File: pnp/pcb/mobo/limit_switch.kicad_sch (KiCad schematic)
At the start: 6 parts, among them J2 X_LIMIT

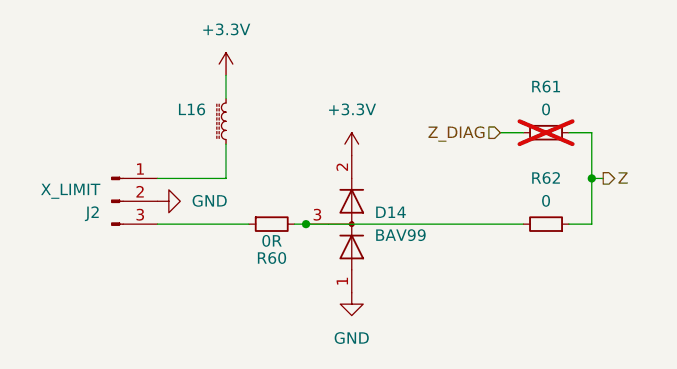
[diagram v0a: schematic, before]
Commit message: Replaced solder jumpers with 0ohm
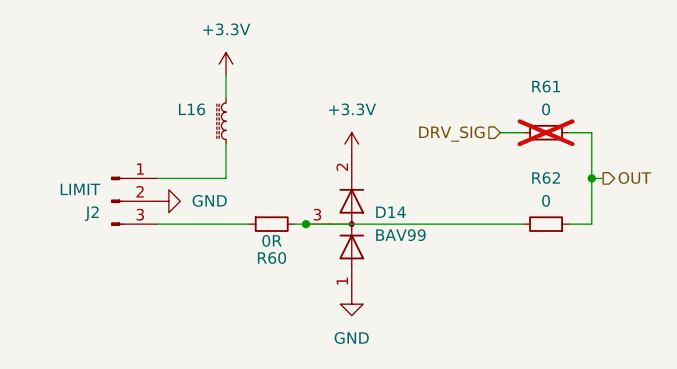
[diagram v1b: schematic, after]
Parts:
- J2: value X_LIMIT -> LIMIT
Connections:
- net Z renamed OUT
- net Z_DIAG renamed DRV_SIG
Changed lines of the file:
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@@
     (stroke (width 0) (type default))
   )
-  (hierarchical_label "Z_DIAG" (shape input) (at 123.19 63.5 180) (fields_autoplaced)
+  (hierarchical_label "DRV_SIG" (shape input) (at 123.19 63.5 180) (fields_autoplaced)
     (effects (font (size 1.27 1.27)) (justify right))
   )
-  (hierarchical_label "Z" (shape output) (at 134.62 68.58 0) (fields_autoplaced)
+  (hierarchical_label "OUT" (shape output) (at 134.62 68.58 0) (fields_autoplaced)
     (effects (font (size 1.27 1.27)) (justify left))
   )
@@
           (reference "R61") (unit 1)
         )
+        (path "/7255cbd1-8d38-4545-be9a-7fc5488ef942/0fa977f6-f205-45fb-8cef-faba0ab4196d"
+          (reference "R73") (unit 1)
+        )
+        (path "/7255cbd1-8d38-4545-be9a-7fc5488ef942/b4f37e88-b6f1-47ba-be3f-95aa26d781b3"
+          (reference "R76") (unit 1)
+        )
       )
     )
@@
           (reference "#PWR083") (unit 1)
         )
+        (path "/7255cbd1-8d38-4545-be9a-7fc5488ef942/0fa977f6-f205-45fb-8cef-faba0ab4196d"
+          (reference "#PWR085") (unit 1)
+        )
+        (path "/7255cbd1-8d38-4545-be9a-7fc5488ef942/b4f37e88-b6f1-47ba-be3f-95aa26d781b3"
+          (reference "#PWR0123") (unit 1)
+        )
       )
     )
@@
           (reference "R62") (unit 1)
         )
+        (path "/7255cbd1-8d38-4545-be9a-7fc5488ef942/0fa977f6-f205-45fb-8cef-faba0ab4196d"
+          (reference "R74") (unit 1)
+        )
+        (path "/7255cbd1-8d38-4545-be9a-7fc5488ef942/b4f37e88-b6f1-47ba-be3f-95aa26d781b3"
+          (reference "R77") (unit 1)
+        )
       )
     )
@@
           (reference "#PWR0117") (unit 1)
         )
+        (path "/7255cbd1-8d38-4545-be9a-7fc5488ef942/0fa977f6-f205-45fb-8cef-faba0ab4196d"
+          (reference "#PWR0122") (unit 1)
+        )
+        (path "/7255cbd1-8d38-4545-be9a-7fc5488ef942/b4f37e88-b6f1-47ba-be3f-95aa26d781b3"
+          (reference "#PWR0126") (unit 1)
+        )
       )
     )
@@
         (path "/7255cbd1-8d38-4545-be9a-7fc5488ef942/02705e7d-b250-4955-94ce-1e1db6770300"
           (reference "#PWR0176") (unit 1)
+        )
+        (path "/7255cbd1-8d38-4545-be9a-7fc5488ef942/0fa977f6-f205-45fb-8cef-faba0ab4196d"
+          (reference "#PWR086") (unit 1)
+        )
+        (path "/7255cbd1-8d38-4545-be9a-7fc5488ef942/b4f37e88-b6f1-47ba-be3f-95aa26d781b3"
+          (reference "#PWR0124") (unit 1)
         )
       )
@@
         (path "/7255cbd1-8d38-4545-be9a-7fc5488ef942/02705e7d-b250-4955-94ce-1e1db6770300"
           (reference "D14") (unit 1)
+        )
+        (path "/7255cbd1-8d38-4545-be9a-7fc5488ef942/0fa977f6-f205-45fb-8cef-faba0ab4196d"
+          (reference "D15") (unit 1)
+        )
+        (path "/7255cbd1-8d38-4545-be9a-7fc5488ef942/b4f37e88-b6f1-47ba-be3f-95aa26d781b3"
+          (reference "D16") (unit 1)
         )
       )
@@
           (reference "R60") (unit 1)
         )
+        (path "/7255cbd1-8d38-4545-be9a-7fc5488ef942/0fa977f6-f205-45fb-8cef-faba0ab4196d"
+          (reference "R72") (unit 1)
+        )
+        (path "/7255cbd1-8d38-4545-be9a-7fc5488ef942/b4f37e88-b6f1-47ba-be3f-95aa26d781b3"
+          (reference "R75") (unit 1)
+        )
       )
     )
@@
         (path "/7255cbd1-8d38-4545-be9a-7fc5488ef942/02705e7d-b250-4955-94ce-1e1db6770300"
           (reference "L16") (unit 1)
+        )
+        (path "/7255cbd1-8d38-4545-be9a-7fc5488ef942/0fa977f6-f205-45fb-8cef-faba0ab4196d"
+          (reference "L14") (unit 1)
+        )
+        (path "/7255cbd1-8d38-4545-be9a-7fc5488ef942/b4f37e88-b6f1-47ba-be3f-95aa26d781b3"
+          (reference "L17") (unit 1)
         )
       )
@@
       (effects (font (size 1.27 1.27)) (justify right))
     )
-    (property "Value" "X_LIMIT" (at 78.74 69.85 0)
+    (property "Value" "LIMIT" (at 78.74 69.85 0)
       (effects (font (size 1.27 1.27)) (justify right))
     )
@@
           (reference "J2") (unit 1)
         )
+        (path "/7255cbd1-8d38-4545-be9a-7fc5488ef942/0fa977f6-f205-45fb-8cef-faba0ab4196d"
+          (reference "J3") (unit 1)
+        )
+        (path "/7255cbd1-8d38-4545-be9a-7fc5488ef942/b4f37e88-b6f1-47ba-be3f-95aa26d781b3"
+          (reference "J4") (unit 1)
+        )
       )
     )
@@
           (reference "#PWR084") (unit 1)
         )
-      )
+        (path "/7255cbd1-8d38-4545-be9a-7fc5488ef942/0fa977f6-f205-45fb-8cef-faba0ab4196d"
+          (reference "#PWR0121") (unit 1)
+        )
+        (path "/7255cbd1-8d38-4545-be9a-7fc5488ef942/b4f37e88-b6f1-47ba-be3f-95aa26d781b3"
+          (reference "#PWR0125") (unit 1)
+        )
+      )

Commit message: Motor driver new Symbol and fix TVS placement
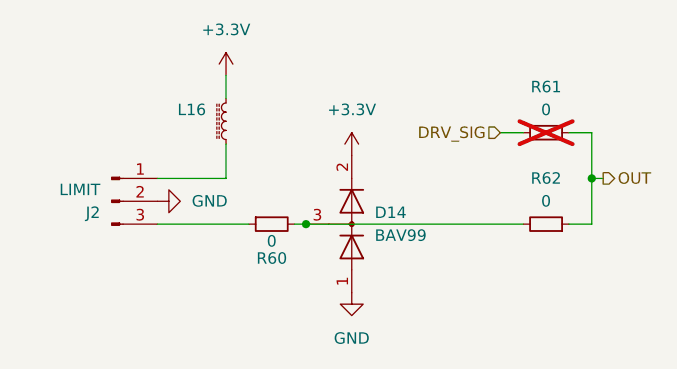
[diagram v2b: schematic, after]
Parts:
- L16: footprint index:L_0805_2012Metric -> Inductor_SMD:L_0805_2012Metric
- R60: value 0R -> 0
- R61, R62: footprint (none) -> Resistor_SMD:R_0805_2012Metric

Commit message: Increased motor driver sense resistor package size
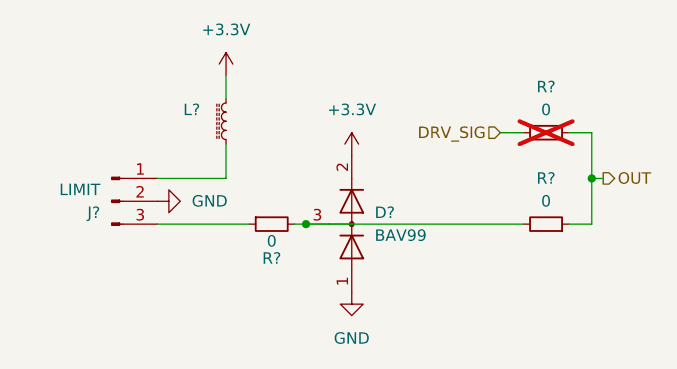
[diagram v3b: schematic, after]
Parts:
- renumbered D14 to D?, J2 to J?, L16 to L?, R61 to R?, R62 to R?, R60 to R?
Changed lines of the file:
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@@
   (symbol (lib_id "Device:R_Small") (at 128.27 63.5 270) (mirror x) (unit 1)
     (in_bom yes) (on_board yes) (dnp yes) (fields_autoplaced)
-    (property "Reference" "R61" (at 128.27 58.42 90)
+    (property "Reference" "R?" (at 128.27 58.42 90)
       (effects (font (size 1.27 1.27)))
     )
@@
   (symbol (lib_name "GND_2") (lib_id "power:GND") (at 85.09 71.12 90) (mirror x) (unit 1)
     (in_bom yes) (on_board yes) (dnp no) (fields_autoplaced)
-    (property "Reference" "#PWR083" (at 91.44 71.12 0)
+    (property "Reference" "#PWR?" (at 91.44 71.12 0)
       (effects (font (size 1.27 1.27)) hide)
     )
@@
   (symbol (lib_id "Device:R_Small") (at 128.27 73.66 270) (mirror x) (unit 1)
     (in_bom yes) (on_board yes) (dnp no) (fields_autoplaced)
-    (property "Reference" "R62" (at 128.27 68.58 90)
+    (property "Reference" "R?" (at 128.27 68.58 90)
       (effects (font (size 1.27 1.27)))
     )
@@
   (symbol (lib_name "GND_1") (lib_id "power:GND") (at 106.68 81.28 0) (mirror y) (unit 1)
     (in_bom yes) (on_board yes) (dnp no) (fields_autoplaced)
-    (property "Reference" "#PWR0117" (at 106.68 87.63 0)
+    (property "Reference" "#PWR?" (at 106.68 87.63 0)
       (effects (font (size 1.27 1.27)) hide)
     )
@@
   (symbol (lib_name "+3.3V_1") (lib_id "power:+3.3V") (at 92.71 57.15 0) (mirror y) (unit 1)
     (in_bom yes) (on_board yes) (dnp no) (fields_autoplaced)
-    (property "Reference" "#PWR0176" (at 92.71 60.96 0)
+    (property "Reference" "#PWR?" (at 92.71 60.96 0)
       (effects (font (size 1.27 1.27)) hide)
     )
@@
   (symbol (lib_id "Diode:BAV99") (at 106.68 73.66 270) (mirror x) (unit 1)
     (in_bom yes) (on_board yes) (dnp no) (fields_autoplaced)
-    (property "Reference" "D14" (at 109.22 72.39 90)
+    (property "Reference" "D?" (at 109.22 72.39 90)
       (effects (font (size 1.27 1.27)) (justify left))
     )
@@
   (symbol (lib_id "Device:R_Small") (at 97.79 73.66 90) (mirror x) (unit 1)
     (in_bom yes) (on_board yes) (dnp no)
-    (property "Reference" "R60" (at 97.79 77.47 90)
+    (property "Reference" "R?" (at 97.79 77.47 90)
       (effects (font (size 1.27 1.27)))
     )
@@
   (symbol (lib_id "Device:L_Ferrite_Small") (at 92.71 62.23 0) (mirror y) (unit 1)
     (in_bom yes) (on_board yes) (dnp no)
-    (property "Reference" "L16" (at 88.9 60.96 0)
+    (property "Reference" "L?" (at 88.9 60.96 0)
       (effects (font (size 1.27 1.27)))
     )
@@
   (symbol (lib_id "Connector:Conn_01x03_Male") (at 80.01 71.12 0) (unit 1)
     (in_bom yes) (on_board yes) (dnp no)
-    (property "Reference" "J2" (at 78.74 72.39 0)
+    (property "Reference" "J?" (at 78.74 72.39 0)
       (effects (font (size 1.27 1.27)) (justify right))
     )
@@
   (symbol (lib_name "+3.3V_1") (lib_id "power:+3.3V") (at 106.68 66.04 0) (mirror y) (unit 1)
     (in_bom yes) (on_board yes) (dnp no) (fields_autoplaced)
-    (property "Reference" "#PWR084" (at 106.68 69.85 0)
-      (effects (font (size 1.27 1.27)) hide)
-    )
+    (property "Reference" "#PWR?" (at 106.68 69.85 0)
+      (effects (font (size 1.27 1.27)) hide)
+    )

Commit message: Mobo parts sourced
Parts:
- removed R?: 0, Resistor_SMD:R_0805_2012Metric, symbol Device:R_Small
- D?: JLCPCB (none) -> C2500; LCSC (none) -> C916421
- J?: JLCPCB C2316 -> C2845452; LCSC C2316 -> C2845452
- L?: JLCPCB (none) -> C1015; LCSC (none) -> C1015; Notes 50Ohm@100Mhz -> (none)
- R? (x2): JLCPCB (none) -> C17477; LCSC (none) -> C17477
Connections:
- net at D?.3 (K), R?.2: now also J?.3 (Pin_3)
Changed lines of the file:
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@@
-    (stroke (width 0) (type default))
-  )
-  (wire (pts (xy 95.25 73.66) (xy 85.09 73.66))
     (stroke (width 0) (type default))
   )
@@
     (stroke (width 0) (type default))
   )
-  (wire (pts (xy 101.6 73.66) (xy 100.33 73.66))
+  (wire (pts (xy 85.09 73.66) (xy 101.6 73.66))
     (stroke (width 0) (type default))
   )
@@
       (effects (font (size 1.27 1.27)) hide)
     )
+    (property "JLCPCB" "C17477" (at 128.27 63.5 0)
+      (effects (font (size 1.27 1.27)) hide)
+    )
+    (property "LCSC" "C17477" (at 128.27 63.5 0)
+      (effects (font (size 1.27 1.27)) hide)
+    )
     (pin "1")
     (pin "2")
@@
       (effects (font (size 1.27 1.27)) hide)
     )
+    (property "JLCPCB" "C17477" (at 128.27 73.66 0)
+      (effects (font (size 1.27 1.27)) hide)
+    )
+    (property "LCSC" "C17477" (at 128.27 73.66 0)
+      (effects (font (size 1.27 1.27)) hide)
+    )
     (pin "1")
     (pin "2")
@@
       (effects (font (size 1.27 1.27)) hide)
     )
+    (property "JLCPCB" "C2500" (at 106.68 73.66 0)
+      (effects (font (size 1.27 1.27)) hide)
+    )
+    (property "LCSC" "C916421" (at 106.68 73.66 0)
+      (effects (font (size 1.27 1.27)) hide)
+    )
     (pin "1")
     (pin "2")
@@
         (path "/7255cbd1-8d38-4545-be9a-7fc5488ef942/b4f37e88-b6f1-47ba-be3f-95aa26d781b3/93becd31-da9a-45fa-a9c6-780d3515a9a1"
           (reference "D16") (unit 1)
-        )
-      )
-    )
-  )
-  (symbol (lib_id "Device:R_Small") (at 97.79 73.66 90) (mirror x) (unit 1)
-    (in_bom yes) (on_board yes) (dnp no)
-    (property "Reference" "R?" (at 97.79 77.47 90)
-      (effects (font (size 1.27 1.27)))
-    )
-    (property "Value" "0" (at 97.79 75.565 90)
-      (effects (font (size 1.27 1.27)))
-    )
-    (property "Footprint" "Resistor_SMD:R_0805_2012Metric" (at 97.79 73.66 0)
-      (effects (font (size 1.27 1.27)) hide)
-    )
-    (property "Datasheet" "~" (at 97.79 73.66 0)
-      (effects (font (size 1.27 1.27)) hide)
-    )
-    (pin "1")
-    (pin "2")
-    (instances
-      (project "mobo"
-        (path "/7255cbd1-8d38-4545-be9a-7fc5488ef942/b4f37e88-b6f1-47ba-be3f-95aa26d781b3"
-          (reference "R?") (unit 1)
-        )
-        (path "/7255cbd1-8d38-4545-be9a-7fc5488ef942/b4f37e88-b6f1-47ba-be3f-95aa26d781b3/1a97bd32-725a-4fe2-8487-743025c8d22a"
-          (reference "R60") (unit 1)
-        )
-        (path "/7255cbd1-8d38-4545-be9a-7fc5488ef942/b4f37e88-b6f1-47ba-be3f-95aa26d781b3/cbcb0479-9830-4167-b571-b924a0062142"
-          (reference "R49") (unit 1)
-        )
-        (path "/7255cbd1-8d38-4545-be9a-7fc5488ef942/b4f37e88-b6f1-47ba-be3f-95aa26d781b3/93becd31-da9a-45fa-a9c6-780d3515a9a1"
-          (reference "R63") (unit 1)
         )
       )
@@
       (effects (font (size 1.27 1.27)) hide)
     )
-    (property "Notes" "50Ohm@100Mhz" (at 92.71 62.23 0)
+    (property "Notes" "" (at 92.71 62.23 0)
+      (effects (font (size 1.27 1.27)) hide)
+    )
+    (property "JLCPCB" "C1015" (at 92.71 62.23 0)
+      (effects (font (size 1.27 1.27)) hide)
+    )
+    (property "LCSC" "C1015" (at 92.71 62.23 0)
       (effects (font (size 1.27 1.27)) hide)
     )
@@
       (effects (font (size 1.27 1.27)) hide)
     )
-    (property "LCSC" "C2316" (at 80.01 71.12 0)
-      (effects (font (size 1.27 1.27)) hide)
-    )
-    (property "JLCPCB" "C2316" (at 80.01 71.12 0)
-      (effects (font (size 1.27 1.27)) hide)
-    )
+    (property "LCSC" "C2845452" (at 80.01 71.12 0)
+      (effects (font (size 1.27 1.27)) hide)
+    )
+    (property "JLCPCB" "C2845452" (at 80.01 71.12 0)
+      (effects (font (size 1.27 1.27)) hide)
+    )
